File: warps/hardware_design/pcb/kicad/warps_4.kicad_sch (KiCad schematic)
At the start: 16 parts

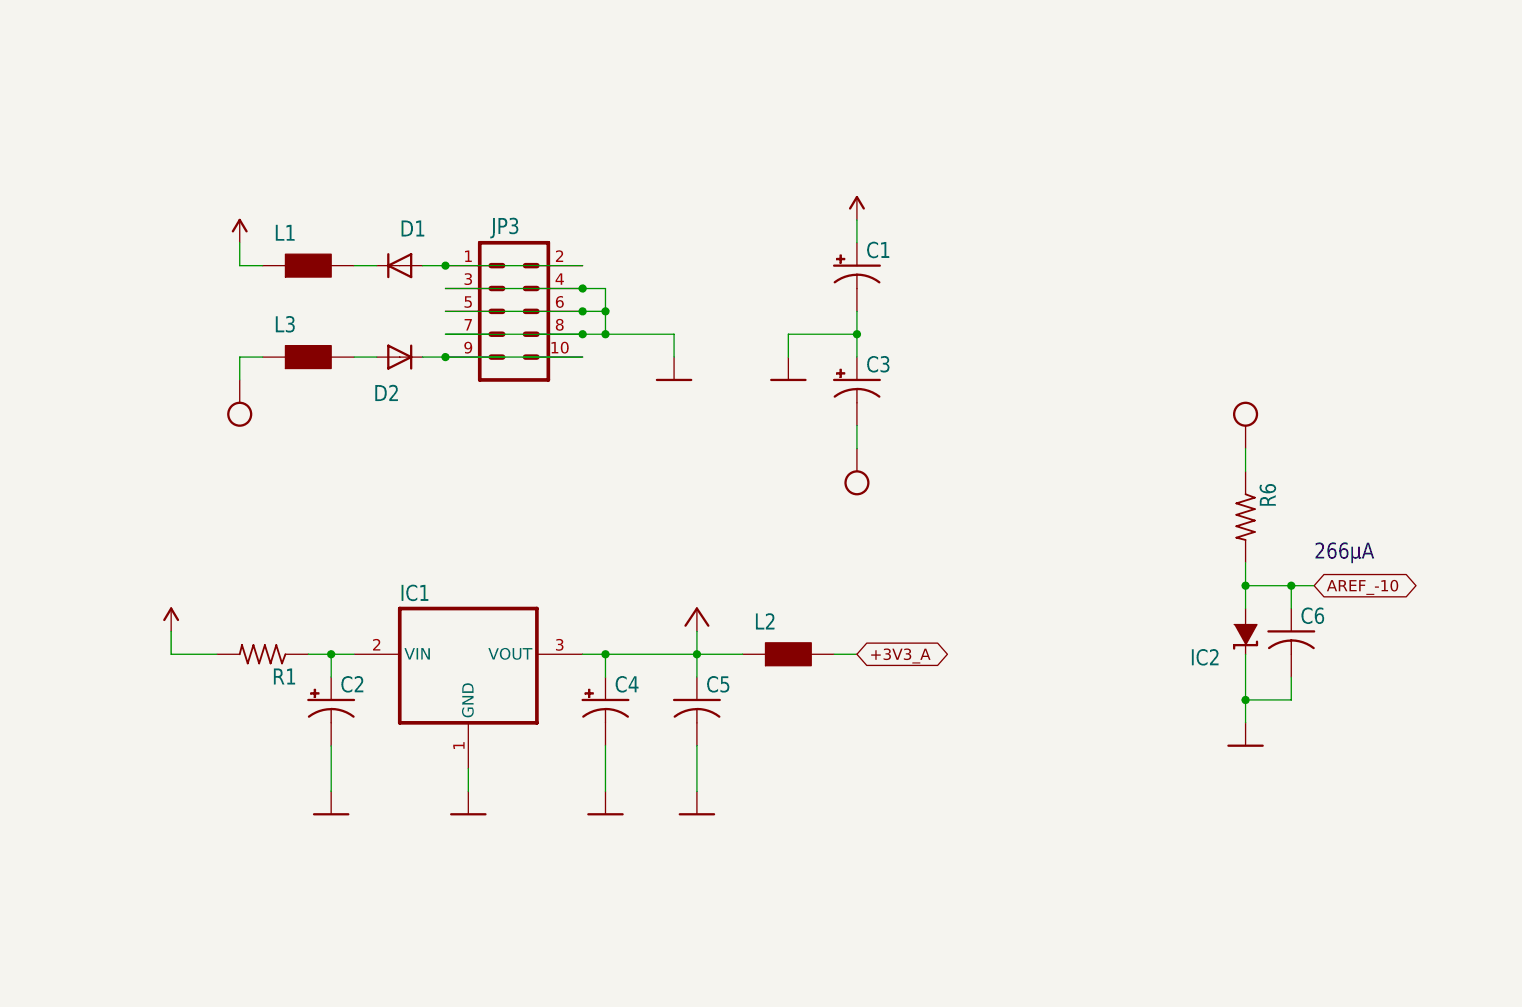
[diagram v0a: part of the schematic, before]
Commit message: warps SMD boot/reset buttons
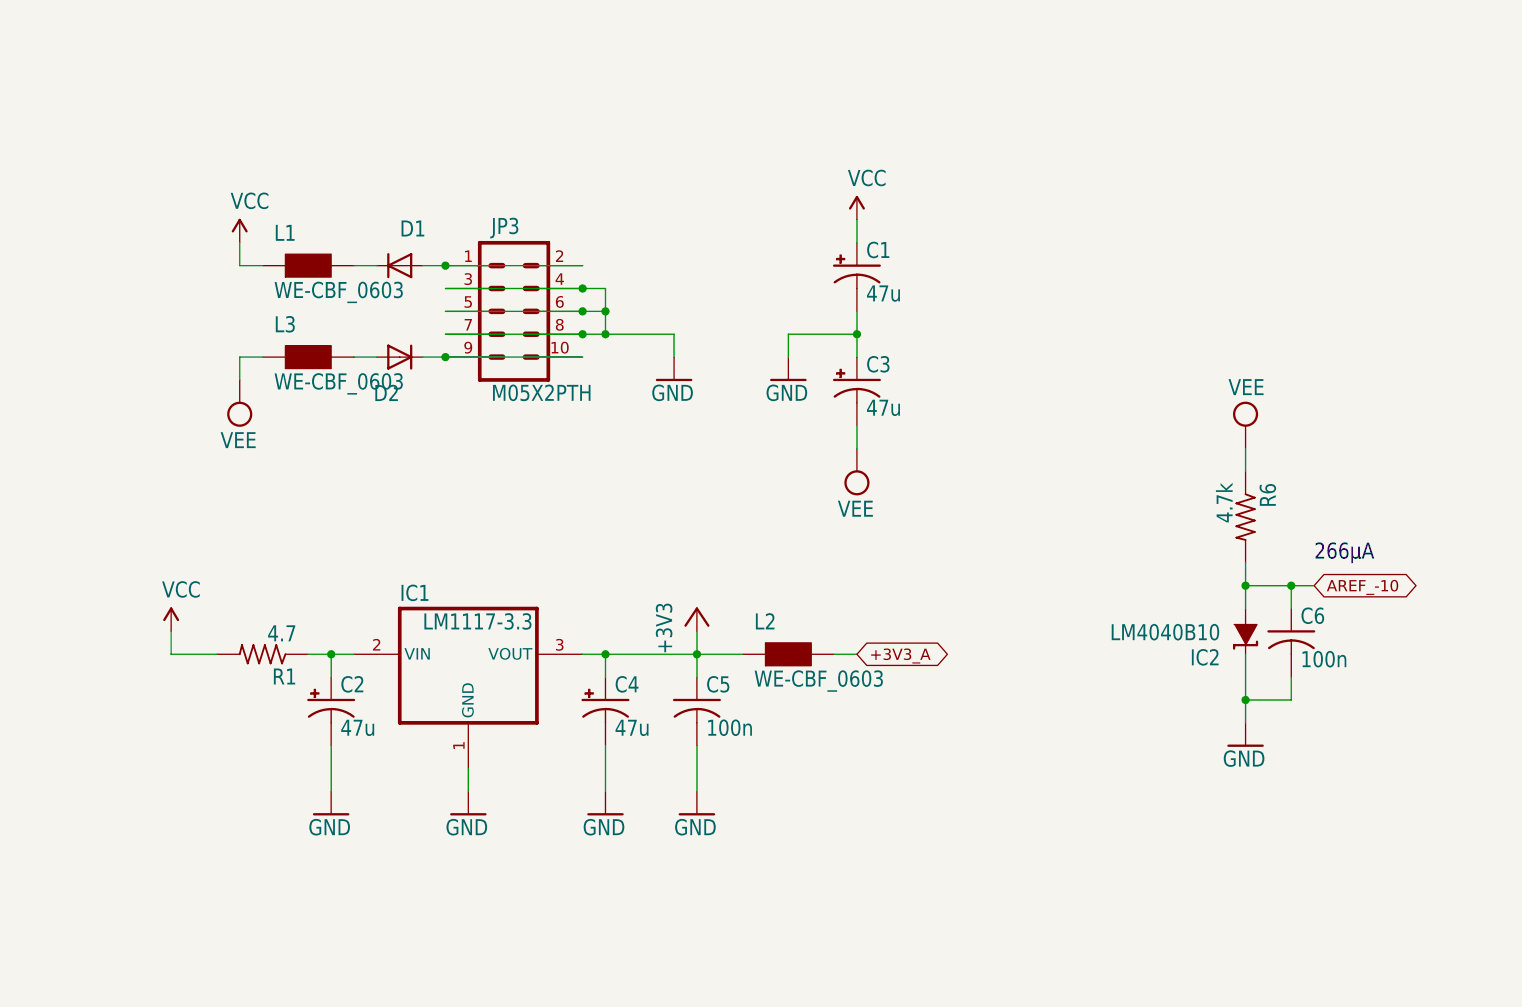
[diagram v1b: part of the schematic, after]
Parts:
- C1, C2, C3, C4: value (none) -> 47u; footprint (none) -> warps:PANASONIC_D
- C5, C6: value (none) -> 100n; footprint (none) -> warps:C0603
- D1, D2: value (none) -> 1N5819HW; footprint (none) -> warps:SOD123
- IC1: value (none) -> LM1117-3.3; footprint (none) -> warps:TO252
- IC2: value (none) -> LM4040B10; footprint (none) -> warps:DBZ_R-PDSO-G3
- JP3: value (none) -> M05X2PTH; footprint (none) -> warps:AVR_ICSP
- L1, L2, L3: value (none) -> WE-CBF_0603; footprint (none) -> warps:0603
- R1: value (none) -> 4.7; footprint (none) -> warps:R1206
- R6: value (none) -> 4.7k; footprint (none) -> warps:R0603
